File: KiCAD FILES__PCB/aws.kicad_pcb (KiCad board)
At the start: 2 copper layers, 228.2 x 91.2 mm, 164 parts, among them J17 B4B-XH-A_LF__SN_, J20 B3B-XH-A_LF__SN_, J21 B3B-XH-A_LF__SN_, J25 Screw_Terminal_01x02, J26 Screw_Terminal_01x02, J27 Screw_Terminal_01x02, J28 B4B-XH-A_LF__SN_, J3 B3B-XH-A_LF__SN_, J32 B3B-XH-A_LF__SN_, J37 B3B-XH-A_LF__SN_, J39 Conn_01x02_Pin, SW6 SW_SPST

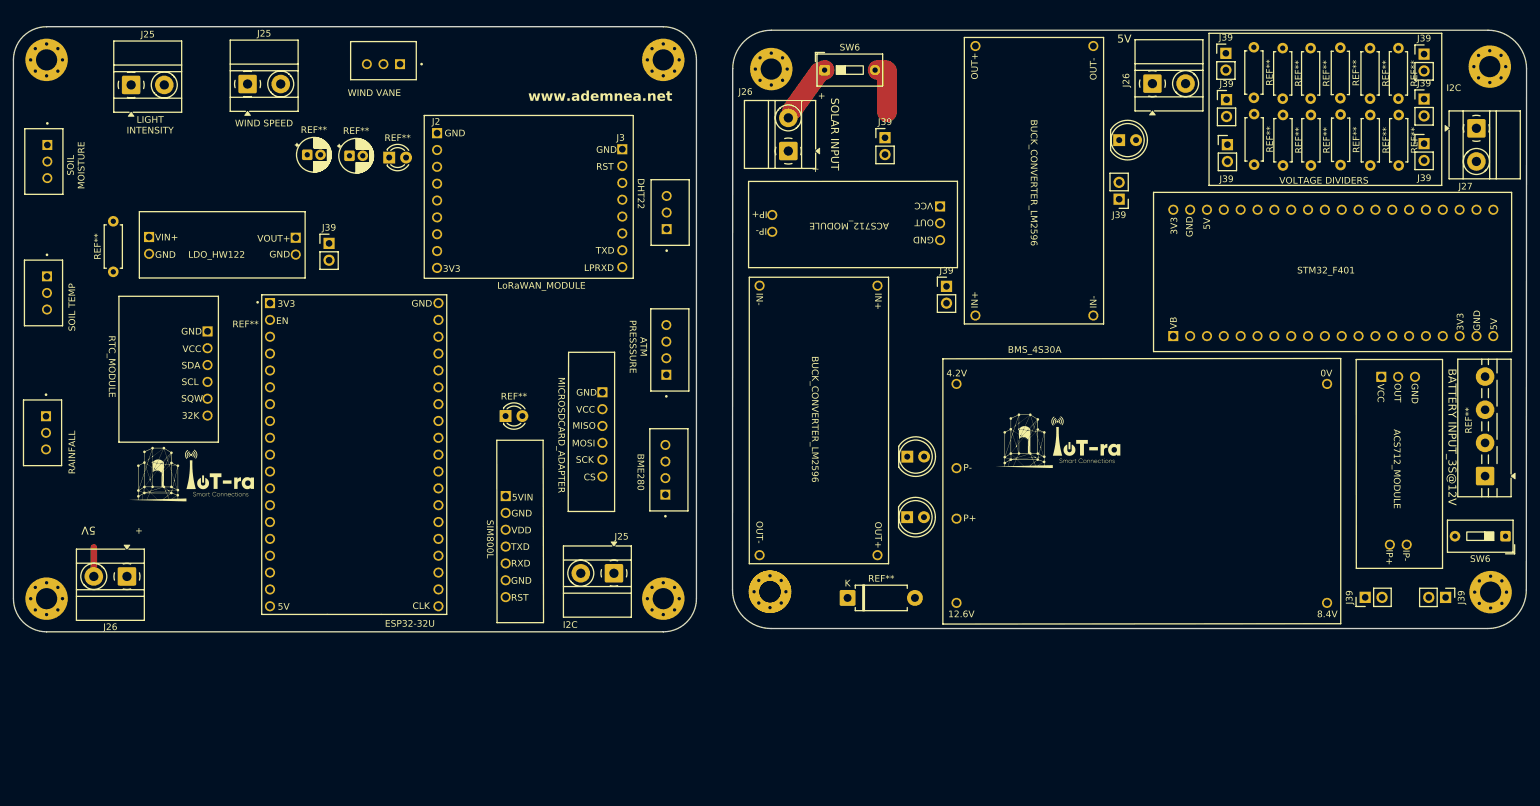
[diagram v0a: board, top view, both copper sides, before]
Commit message: [3rd] Updated layout and routed the Power Board.
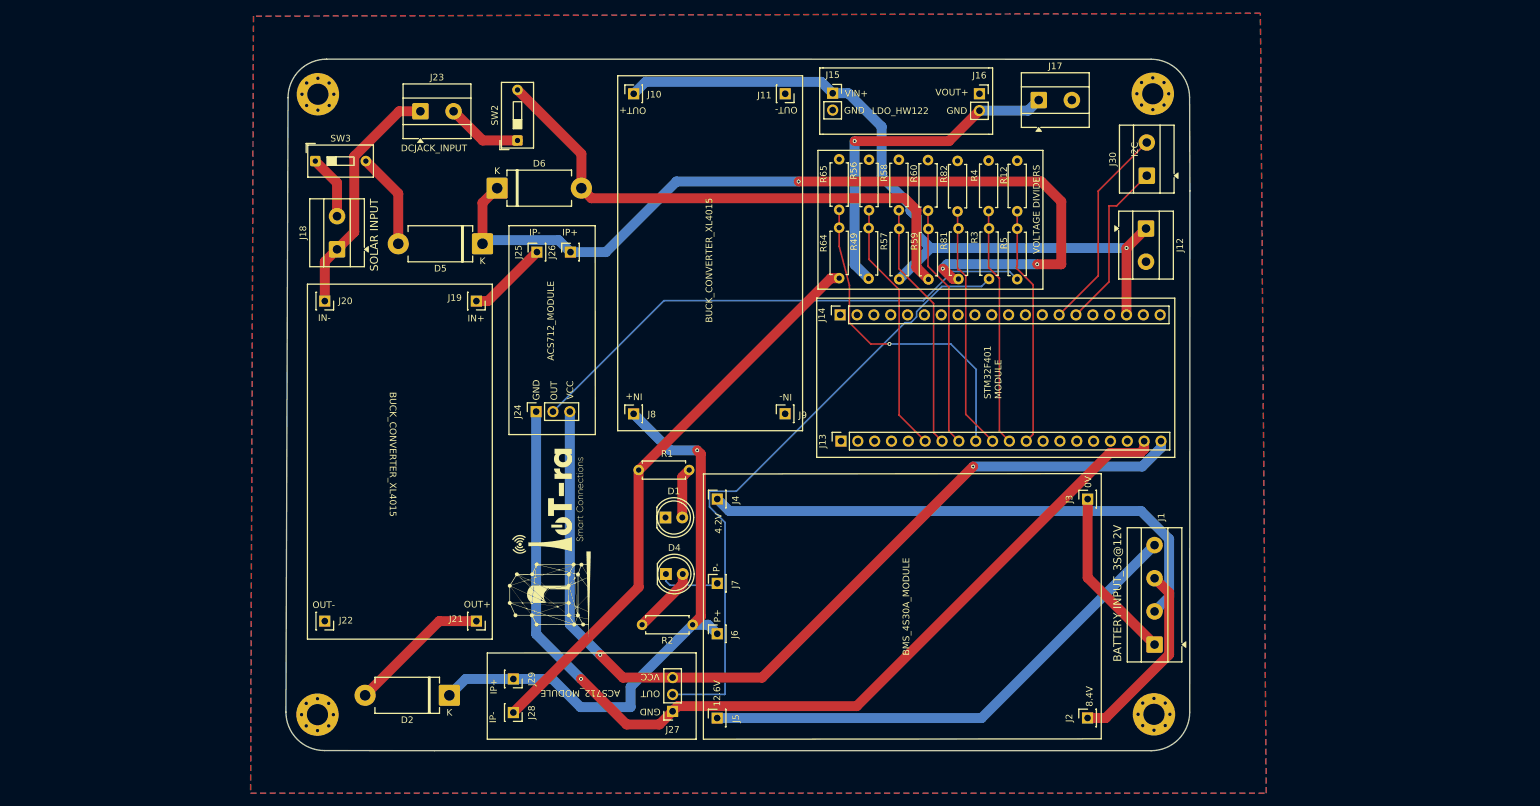
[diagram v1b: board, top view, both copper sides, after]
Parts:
- removed ? (x105): , 
- removed the J25 at (71.0, 45.7)
- removed the J25 at (53.4, 45.9)
- removed the J25 at (126.2, 119.5)
- removed the J26 at (207.4, 45.7)
- removed the J26 at (152.5, 55.8)
- removed the J26 at (52.8, 120.0)
- removed J32, J37: B3B-XH-A_LF__SN_, B3B-XH-A_LF__SN_:JST_B3B-XH-A_LF__SN_
- removed J39 (x12): Conn_01x02_Pin, Connector_PinHeader_2.54mm:PinHeader_1x02_P2.54mm_Vertical
- removed the REF** at (50.7, 74.1)
- removed the REF** at (202.4, 54.2)
- removed the REF** at (170.4, 111.1)
- removed the REF** at (80.0, 56.4)
- removed the REF** at (222.7, 40.2)
- removed the REF** at (240.2, 40.3)
- removed the REF** at (40.7, 123.3)
- removed the REF** at (231.3, 40.3)
- removed the REF** at (87.1, 101.6)
- removed the REF** at (149.8, 122.3)
- removed the REF** at (227.1, 40.3)
- removed the REF** at (240.3, 50.4)
- removed the REF** at (235.8, 40.3)
- removed the REF** at (92.3, 56.8)
- removed the REF** at (161.5, 123.2)
- removed the REF** at (170.5, 101.9)
- removed the REF** at (40.7, 42.1)
- removed the REF** at (257.6, 104.9)
- removed the REF** at (244.6, 50.4)
- removed the REF** at (231.3, 50.4)
- removed the REF** at (235.8, 50.3)
- removed the REF** at (86.3, 56.6)
- removed the REF** at (227.1, 50.4)
- removed the REF** at (222.8, 50.3)
- removed the REF** at (244.5, 40.3)
- removed the REF** at (133.7, 123.3)
- removed the REF** at (109.9, 95.8)
- removed the REF** at (133.7, 42.1)
- removed SW6 (x2): SW_SPST, Button_Switch_THT:SW_DIP_SPSTx01_Slide_9.78x4.72mm_W7.62mm_P2.54mm
- added D1: LED, LED_THT:LED_D5.0mm, F.Cu at (134.0, 111.1)
- added D2: 1N5822, Diode_THT:D_DO-201AD_P12.70mm_Horizontal, F.Cu at (101.4, 137.9)
- added D4: LED, LED_THT:LED_D5.0mm, F.Cu at (134.1, 119.6)
- added D5: 1N5822, Diode_THT:D_DO-201AD_P12.70mm_Horizontal, F.Cu at (106.4, 69.8)
- added D6: 1N5822, Diode_THT:D_DO-201AD_P12.70mm_Horizontal, F.Cu at (108.6, 61.4)
- added J1: BATTERY_INPUT, TerminalBlock_MetzConnect:TerminalBlock_MetzConnect_Type055_RT01504HDWU_1x04_P5.00mm_Horizontal, F.Cu at (207.8, 130.3)
- added J10: OUT+, Connector_PinSocket_2.54mm:PinSocket_1x01_P2.54mm_Vertical, F.Cu at (129.2, 47.2)
- added J11: OUT-, Connector_PinSocket_2.54mm:PinSocket_1x01_P2.54mm_Vertical, F.Cu at (152.1, 47.2)
- added J12: 5V_OUTPUT, TerminalBlock_MetzConnect:TerminalBlock_MetzConnect_Type055_RT01502HDWU_1x02_P5.00mm_Horizontal, F.Cu at (206.5, 67.5)
- added J13: Conn_01x20_Socket, Connector_PinSocket_2.54mm:PinSocket_1x20_P2.54mm_Vertical, F.Cu at (160.5, 99.6)
- added J14: Conn_01x20_Socket, Connector_PinSocket_2.54mm:PinSocket_1x20_P2.54mm_Vertical, F.Cu at (160.3, 80.6)
- added J15: IN, Connector_PinSocket_2.54mm:PinSocket_1x02_P2.54mm_Vertical, F.Cu at (159.2, 47.1)
- added J16: OUT, Connector_PinSocket_2.54mm:PinSocket_1x02_P2.54mm_Vertical, F.Cu at (181.3, 47.2)
- added J18: SOLAR_INPUT, TerminalBlock_MetzConnect:TerminalBlock_MetzConnect_Type055_RT01502HDWU_1x02_P5.00mm_Horizontal, F.Cu at (84.5, 70.7)
- added J19: IN+, Connector_PinSocket_2.54mm:PinSocket_1x01_P2.54mm_Vertical, F.Cu at (105.5, 78.5)
- added J2: 8.4V, Connector_PinSocket_2.54mm:PinSocket_1x01_P2.54mm_Vertical, F.Cu at (197.7, 141.3)
- added J22: OUT-, Connector_PinSocket_2.54mm:PinSocket_1x01_P2.54mm_Vertical, F.Cu at (82.6, 126.7)
- added J23: DCJACK_INPUT, TerminalBlock_MetzConnect:TerminalBlock_MetzConnect_Type055_RT01502HDWU_1x02_P5.00mm_Horizontal, F.Cu at (97.0, 49.9)
- added J24: Conn_01x03_Socket, Connector_PinSocket_2.54mm:PinSocket_1x03_P2.54mm_Vertical, F.Cu at (114.5, 95.1)
- added J25: 12.6V, Connector_PinSocket_2.54mm:PinSocket_1x01_P2.54mm_Vertical, F.Cu at (114.6, 71.1)
- added J26: 12.6V, Connector_PinSocket_2.54mm:PinSocket_1x01_P2.54mm_Vertical, F.Cu at (119.7, 71.1)
- added J29: 12.6V, Connector_PinSocket_2.54mm:PinSocket_1x01_P2.54mm_Vertical, F.Cu at (111.1, 135.5)
- added J30: I2C, TerminalBlock_MetzConnect:TerminalBlock_MetzConnect_Type055_RT01502HDWU_1x02_P5.00mm_Horizontal, F.Cu at (206.6, 59.6)
- added J4: 4.2V, Connector_PinSocket_2.54mm:PinSocket_1x01_P2.54mm_Vertical, F.Cu at (141.8, 108.3)
- added J5: 12.6V, Connector_PinSocket_2.54mm:PinSocket_1x01_P2.54mm_Vertical, F.Cu at (141.8, 141.4)
- added J6: P+, Connector_PinSocket_2.54mm:PinSocket_1x01_P2.54mm_Vertical, F.Cu at (141.8, 128.6)
- added J7: P-, Connector_PinSocket_2.54mm:PinSocket_1x01_P2.54mm_Vertical, F.Cu at (141.8, 121.0)
- added J8: IN+, Connector_PinSocket_2.54mm:PinSocket_1x01_P2.54mm_Vertical, F.Cu at (129.2, 95.5)
- added J9: IN-, Connector_PinSocket_2.54mm:PinSocket_1x01_P2.54mm_Vertical, F.Cu at (152.0, 95.5)
- added R1: 4.7k, Resistor_THT:R_Axial_DIN0207_L6.3mm_D2.5mm_P7.62mm_Horizontal, F.Cu at (130.0, 104.0)
- added R12: 13k, Resistor_THT:R_Axial_DIN0207_L6.3mm_D2.5mm_P7.62mm_Horizontal, F.Cu at (187.0, 64.9)
- added R2: 4.7k, Resistor_THT:R_Axial_DIN0207_L6.3mm_D2.5mm_P7.62mm_Horizontal, F.Cu at (138.1, 127.3)
- added R3: 10K, Resistor_THT:R_Axial_DIN0207_L6.3mm_D2.5mm_P7.62mm_Horizontal, F.Cu at (182.8, 75.1)
- added R4: 13k, Resistor_THT:R_Axial_DIN0207_L6.3mm_D2.5mm_P7.62mm_Horizontal, F.Cu at (182.7, 64.9)
- added R49: 10K, Resistor_THT:R_Axial_DIN0207_L6.3mm_D2.5mm_P7.62mm_Horizontal, F.Cu at (164.6, 75.1)
- added R5: 10K, Resistor_THT:R_Axial_DIN0207_L6.3mm_D2.5mm_P7.62mm_Horizontal, F.Cu at (187.0, 75.2)
- added R56: 20k, Resistor_THT:R_Axial_DIN0207_L6.3mm_D2.5mm_P7.62mm_Horizontal, F.Cu at (164.7, 64.8)
- added R57: 10K, Resistor_THT:R_Axial_DIN0207_L6.3mm_D2.5mm_P7.62mm_Horizontal, F.Cu at (169.2, 75.2)
- added R58: 13k, Resistor_THT:R_Axial_DIN0207_L6.3mm_D2.5mm_P7.62mm_Horizontal, F.Cu at (169.2, 64.8)
- added R59: 10K, Resistor_THT:R_Axial_DIN0207_L6.3mm_D2.5mm_P7.62mm_Horizontal, F.Cu at (173.7, 75.2)
- added R60: 1.5K, Resistor_THT:R_Axial_DIN0207_L6.3mm_D2.5mm_P7.62mm_Horizontal, F.Cu at (173.6, 64.8)
- added R64: 10K, Resistor_THT:R_Axial_DIN0207_L6.3mm_D2.5mm_P7.62mm_Horizontal, F.Cu at (160.2, 75.0)
- added R65: 2k, Resistor_THT:R_Axial_DIN0207_L6.3mm_D2.5mm_P7.62mm_Horizontal, F.Cu at (160.2, 64.7)
- added R81: 10K, Resistor_THT:R_Axial_DIN0207_L6.3mm_D2.5mm_P7.62mm_Horizontal, F.Cu at (178.2, 75.1)
- added R82: 1.2K, Resistor_THT:R_Axial_DIN0207_L6.3mm_D2.5mm_P7.62mm_Horizontal, F.Cu at (178.0, 65.0)
- added REF**: MountingHole_3.2mm_M3_Pad_Via, MountingHole:MountingHole_3.2mm_M3_Pad_Via, F.Cu at (81.5, 140.8)
- added SW2: SW_SPST, Button_Switch_THT:SW_DIP_SPSTx01_Slide_9.78x4.72mm_W7.62mm_P2.54mm, F.Cu at (111.7, 54.3)
- added SW3: SW_SPST, Button_Switch_THT:SW_DIP_SPSTx01_Slide_9.78x4.72mm_W7.62mm_P2.54mm, F.Cu at (81.2, 57.4)
- J17: value B4B-XH-A_LF__SN_ -> 3.3V_OUTPUT; footprint B4B-XH-A_LF__SN_:JST_B4B-XH-A_LF__SN_ -> TerminalBlock_MetzConnect:TerminalBlock_MetzConnect_Type055_RT01502HDWU_1x02_P5.00mm_Horizontal
- J20: value B3B-XH-A_LF__SN_ -> IN-; footprint B3B-XH-A_LF__SN_:JST_B3B-XH-A_LF__SN_ -> Connector_PinSocket_2.54mm:PinSocket_1x01_P2.54mm_Vertical
- J21: value B3B-XH-A_LF__SN_ -> OUT+; footprint B3B-XH-A_LF__SN_:JST_B3B-XH-A_LF__SN_ -> Connector_PinSocket_2.54mm:PinSocket_1x01_P2.54mm_Vertical
- J27: value Screw_Terminal_01x02 -> Conn_01x03_Socket; footprint TerminalBlock_MetzConnect:TerminalBlock_MetzConnect_Type011_RT05502HBWC_1x02_P5.00mm_Horizontal -> Connector_PinSocket_2.54mm:PinSocket_1x03_P2.54mm_Vertical
- J28: value B4B-XH-A_LF__SN_ -> 12.6V; footprint B4B-XH-A_LF__SN_:JST_B4B-XH-A_LF__SN_ -> Connector_PinSocket_2.54mm:PinSocket_1x01_P2.54mm_Vertical
- J3: value B3B-XH-A_LF__SN_ -> 0V; footprint B3B-XH-A_LF__SN_:JST_B3B-XH-A_LF__SN_ -> Connector_PinSocket_2.54mm:PinSocket_1x01_P2.54mm_Vertical
- moved J3 157.9 mm to (197.7, 108.3)
- moved J27 149.7 mm to (135.1, 140.3), turned to 180 degrees
- moved J21 81.9 mm to (105.5, 126.7), turned to -90 degrees
- moved J17 78.9 mm to (190.3, 48.2), turned to 0 degrees
- moved REF** 68.5 mm to (81.6, 47.3)
- moved J28 59.6 mm to (111.1, 140.5)
- moved REF** 54.0 mm to (207.7, 140.8)
- moved REF** 51.0 mm to (207.5, 47.2)
- moved J20 47.3 mm to (82.6, 78.5), turned to -90 degrees
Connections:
- J17 pad 1: (no net) -> +3.3V
- J17 pad 2: (no net) -> GND
- J20 pad 1: (no net) -> /power board/DC-
- J21 pad 1: (no net) -> Net-(D2-A)
- J27 pad 1: (no net) -> /power board/GND1
- J27 pad 2: (no net) -> /power board/BATT2_TEST
- J28 pad 1: +3.3V_LORA -> /power board/BATT_TEST
- J3 pad 1: (no net) -> /power board/B-
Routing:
- net /power board/GND1: track 0.00 -> 149.3 mm, vias 0 -> 1
- net /power board/5V1: track 0.00 -> 139.9 mm, vias 0 -> 2
- net /power board/IP+1: track 0.00 -> 133.9 mm, vias 0 -> 3
- net +5V: track 0.00 -> 112.8 mm, vias 0 -> 1
- net /power board/BATT2_TEST: track 0.00 -> 95.4 mm
- net /power board/BMS_P+: track 0.00 -> 89.6 mm, vias 0 -> 1
- net /power board/BATT_TEST: track 0.00 -> 86.6 mm
- net /power board/B1: track 0.00 -> 82.5 mm
- net /power board/DCJACK_TEST: track 0.00 -> 81.9 mm
- net /power board/SOLAR2_TEST: track 0.00 -> 79.2 mm
- net /power board/B+: track 0.00 -> 76.8 mm
- net +3.3V: track 0.00 -> 51.9 mm, vias 0 -> 1
- net /power board/5V_INPUT: track 0.00 -> 38.6 mm
- net /power board/BATT_INPUT: track 0.00 -> 38.4 mm, vias 0 -> 1
- net /power board/3V3_INPUT: track 0.00 -> 38.3 mm
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- added copper zone on B.Cu, net GND
- added copper zone on F.Cu, net GND
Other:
- board size 228.2 x 91.2 mm -> 136.3 x 104.3 mm
- board text added: "BMS_4S30A_MODULE"
- board text added: "BUCK_CONVERTER_XL4015"
- board text added: "DCJACK_INPUT"
- board text added: "STM32F401 MODULE"
- board text removed: "+"
- board text removed: "32K"
- board text removed: "3V3"
- board text removed: "5V"
- board text removed: "5VIN"
- board text removed: "ATM PRESSSURE"
- board text removed: "AWS Gen4 V1, 2025"
- board text removed: "BME280"
- board text removed: "BMS_4S30A"
- board text removed: "BUCK_CONVERTER_LM2596"
- board text removed: "CLK"
- board text removed: "CS"
- board text removed: "DHT22"
- board text removed: "EN"
- board text removed: "ESP32-32U"
- board text removed: "GATE WAY BOARD"
- board text removed: "J2"
- board text removed: "J3"
- board text removed: "LIGHT INTENSITY"
- board text removed: "LPRXD"
- board text removed: "LoRaWAN_MODULE"
- board text removed: "MICROSDCARD_ADAPTER"
- board text removed: "MISO"
- board text removed: "MOSI"
- board text removed: "RAINFALL"
- board text removed: "RST"
- board text removed: "RTC_MODULE"
- board text removed: "RXD"
- board text removed: "SCK"
- board text removed: "SCL"
- board text removed: "SDA"
- board text removed: "SIM800L"
- board text removed: "SOIL MOISTURE"
- board text removed: "SOIL TEMP"
- board text removed: "SQW"
- board text removed: "STM32_F401"
- board text removed: "TXD"
- board text removed: "VB"
- board text removed: "VDD"
- board text removed: "WIND SPEED"
- board text removed: "WIND VANE"
